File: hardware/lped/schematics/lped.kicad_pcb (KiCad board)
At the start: 4 copper layers, 14 x 14 mm, 30 parts, among them J1 3V3, J10 SWDIO, J2 DOCK_BUTTON, J3 DOCK_CONN, J4 DOCK_LED, J5 GND, J6 ~{RESET}, J9 SWDCLK, U1 nRF52810-QCxx, U2 FXLS8974CF, Y1 32MHz

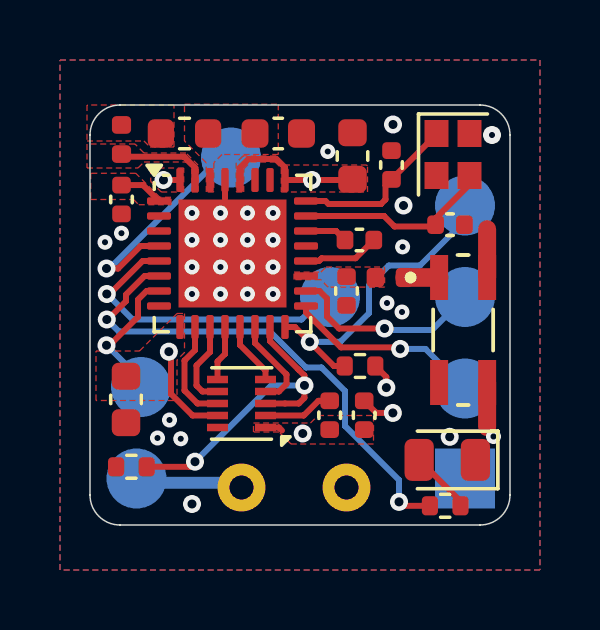
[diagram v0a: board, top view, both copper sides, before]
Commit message: feat(hardware)!: v2 of LPED PCB
* Changed MCU to nRF52833 (from nRF52810)
* Added second LED
* Used specialized filter instead of discrete components for ANT
* Removed unnecessary pull-down resistor from miso
* Removed DOCK_BTN
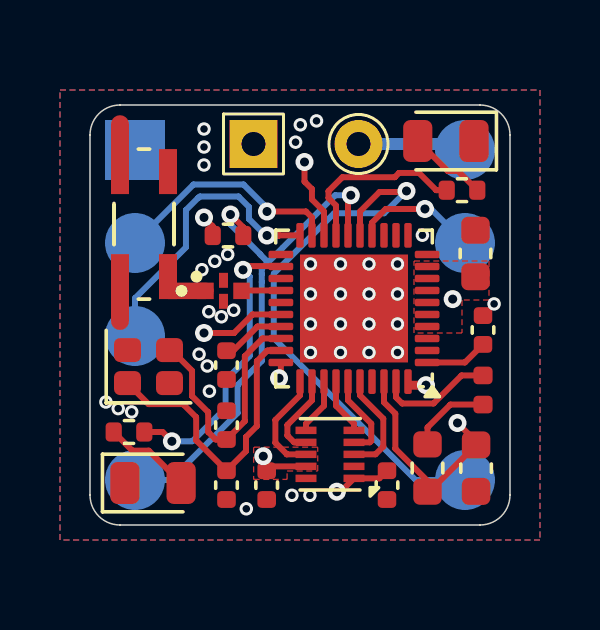
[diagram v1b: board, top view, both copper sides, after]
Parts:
- removed C10: 0u1, Capacitor_SMD:C_0402_1005Metric
- removed C11: 1u, Capacitor_SMD:C_0402_1005Metric
- removed the C3 at (166.1, 72.5)
- removed the J2 at (157.7, 79.9)
- removed L1: 3n9, Inductor_SMD:L_0402_1005Metric
- removed L2: 10u, Inductor_SMD:L_0603_1608Metric
- removed R5: 10k, Resistor_SMD:R_0402_1005Metric
- added C1: 12pF, Capacitor_SMD:C_0402_1005Metric, F.Cu at (160.6, 81.2)
- added D2: LED, Diode_SMD:D_0805_2012Metric, F.Cu at (167.9, 71.7)
- added F1: 2450FM07B0037, RF_Filter:FIL_2450FM07D0034T, F.Cu at (160.4, 76.7)
- added L4: 15n, Inductor_SMD:L_0402_1005Metric, F.Cu at (169.1, 80.0)
- added R3: 2k1, Resistor_SMD:R_0402_1005Metric, F.Cu at (168.4, 73.3)
- C5: value 100p -> 0u1
- C6: value 0p8 -> 100p
- C7: footprint Capacitor_SMD:C_0603_1608Metric -> Capacitor_SMD:C_0402_1005Metric
- C8: value 4u7 -> 1u
- C9: value 1u -> 4u7
- L3: value 15n -> 10u; footprint Inductor_SMD:L_0402_1005Metric -> Inductor_SMD:L_0603_1608Metric
- U1: value nRF52810-QCxx -> nRF52833_QDxx; footprint Package_DFN_QFN:QFN-32-1EP_5x5mm_P0.5mm_EP3.6x3.6mm -> Package_DFN_QFN:QFN-40-1EP_5x5mm_P0.4mm_EP3.6x3.6mm
- moved J7 15.5 mm to (157.5, 72.0)
- moved J4 15.5 mm to (168.5, 72.0)
- moved L3 15.0 mm to (167.2, 82.6), turned to 90 degrees
- moved J1 14.3 mm to (157.5, 83.0)
- moved C4 12.8 mm to (169.1, 78.0), turned to -90 degrees
- moved Y1 12.4 mm to (157.9, 79.2), turned to 0 degrees
- moved C7 12.3 mm to (165.9, 83.2), turned to -90 degrees
- moved C8 11.9 mm to (168.9, 82.6)
- moved C3 11.5 mm to (161.4, 71.8)
- moved C2 11.4 mm to (160.6, 83.2), turned to 90 degrees
- moved AE1 11.2 mm to (157.8, 74.5), turned to -90 degrees
- moved J3 11.1 mm to (157.5, 75.1)
- moved J2 11.1 mm to (157.5, 78.2)
- moved R2 10.8 mm to (157.3, 81.4), turned to 180 degrees
- moved D1 9.84 mm to (158.1, 83.1), turned to 0 degrees
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- renumbered C1 to C3, J6 to J1, J9 to J2, J10 to J3, J1 to J4, J3 to J5, J4 to J6, J5 to J7
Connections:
- C2 pad 2: /XC1 -> /XC2
- C5 pad 1: Earth -> +3V3
- C5 pad 2: /DEC3 -> Earth
- C6 pad 1: /ANT -> Earth
- C6 pad 2: Earth -> /DEC3
- C7 pad 1: Earth -> +3V3
- C7 pad 2: /DEC4 -> Earth
- C8 pad 2: +3V3 -> /DEC4
- C9 pad 1: +3V3 -> Earth
- C9 pad 2: Earth -> +3V3
- L3 pad 1: Net-(L2-Pad2) -> /DEC4
- L3 pad 2: Net-(U1-DCC) -> Net-(L3-Pad2)
- R2 pad 1: /LED -> /LED2
- U1 pad 10: /Accelerometer/INT1 -> Earth
- U1 pad 11: /Accelerometer/CSB -> unconnected-(U1-DECUSB-Pad11)
- U1 pad 12: /Accelerometer/INT2 -> unconnected-(U1-D--Pad12)
- U1 pad 13: /Accelerometer/SCL -> unconnected-(U1-D+-Pad13)
- U1 pad 14: /Accelerometer/MOSI -> /DOCK_CONN
- U1 pad 15: /Accelerometer/MISO -> /DOCK_LED
- U1 pad 17: /SWDCLK -> /LED1
- U1 pad 18: /SWDIO -> +3V3
- U1 pad 19: /ANT -> /SWDIO
- U1 pad 20: Earth -> /SWDCLK
- U1 pad 22: /DEC3 -> /LED2
- U1 pad 23: /XC1 -> unconnected-(U1-NFC2/P0.10-Pad23)
- U1 pad 24: /XC2 -> /ANT
- U1 pad 25: +3V3 -> Earth
- U1 pad 26: unconnected-(U1-P0.25-Pad26) -> /DEC4
- U1 pad 27: unconnected-(U1-P0.28/AIN4-Pad27) -> /DEC3
- U1 pad 28: +3V3 -> /XC1
- U1 pad 29: Earth -> /XC2
- U1 pad 30: /DEC4 -> +3V3
- U1 pad 31: Net-(U1-DCC) -> /Accelerometer/INT1
- U1 pad 32: +3V3 -> /Accelerometer/CSB
- U1 pad 33: Earth -> /Accelerometer/INT2
- U1 pad 4: /DOCK_CONN -> +3V3
- U1 pad 5: /DOCK_LED -> unconnected-(U1-AIN3/P0.05-Pad5)
- U1 pad 6: /LED -> unconnected-(U1-P1.09-Pad6)
- U1 pad 7: /DOCK_BUTTON -> unconnected-(U1-P0.11-Pad7)
- U1 pad 8: /BUZZER -> +3V3
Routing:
- net /DEC4: track 0.00 -> 26.1 mm, vias 0 -> 2
- net /LED: track 16.9 -> 0.00 mm, vias 2 -> 0
- net /LED2: track 0.00 -> 9.65 mm, vias 0 -> 2
- net /DOCK_LED: track 10.5 -> 18.7 mm
- net /~{RESET}: track 10.4 -> 18.0 mm, vias 1 -> 2
- net /Accelerometer/MISO: track 10.6 -> 3.57 mm, vias 2 -> 0
- net Earth: track 9.74 -> 3.06 mm, vias 32 -> 39
- net /LED1: track 0.00 -> 6.01 mm
- net +3V3: track 35.6 -> 41.5 mm, vias 5 -> 7
- net /DOCK_BUTTON: track 4.71 -> 0.00 mm, vias 1 -> 0
- net /XC2: track 5.66 -> 9.81 mm
- net /DOCK_CONN: track 7.74 -> 4.18 mm
- net /SWDCLK: track 6.57 -> 9.66 mm
- net Net-(L3-Pad2): track 0.00 -> 2.73 mm
- net Net-(D2-A): track 0.00 -> 2.66 mm
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- removed copper zone on F.Cu, net /ANT
- removed copper zone on F.Cu, net /DEC1
- removed copper zone on F.Cu, net /DEC4
- removed copper zone on F.Cu, net Net-(L2-Pad2)
- removed copper zone on F.Cu, net Net-(U1-DCC)
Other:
- board text added: "CON"
- board text added: "V2.0"
- board text added: "~{RST}"
- board text removed: "BTN"
- board text removed: "CONN"
- board text removed: "RESET"
- board text removed: "V1.0"

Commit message: feat(hardware): replaced LEDs on dice
* Replaced two red LEDs with single RGB LED (LTRB37G-4R4S)
* Added more ground vias
* Removed DOCK_LED
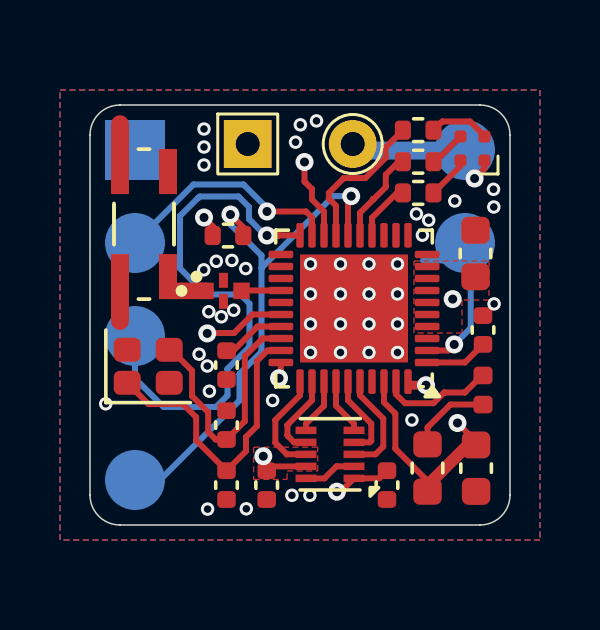
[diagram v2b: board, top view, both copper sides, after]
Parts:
- removed D1, D2: LED, Diode_SMD:D_0805_2012Metric
- removed J6: DOCK_LED, TestPoint:TestPoint_Pad_D2.0mm
- removed R2, R3: 2k1, Resistor_SMD:R_0402_1005Metric
- added D3: LED_RGBA, LED_SMD:LED_Wurth_150044M155260, F.Cu at (168.8, 72.0)
- added R4: 1k, Resistor_SMD:R_0402_1005Metric, F.Cu at (166.9, 73.4)
- added R5: 1k, Resistor_SMD:R_0402_1005Metric, F.Cu at (166.9, 72.4)
- added R6: 1k, Resistor_SMD:R_0402_1005Metric, F.Cu at (166.9, 71.3)
- moved C3 0.19 mm to (161.3, 71.8)
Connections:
- U1 pad 14: /DOCK_CONN -> /LED_R
- U1 pad 15: /DOCK_LED -> /LED_B
- U1 pad 17: /LED1 -> /LED_G
- U1 pad 2: unconnected-(U1-XL1/P0.00-Pad2) -> /DOCK_CONN
- U1 pad 22: /LED2 -> unconnected-(U1-NFC1/P0.09-Pad22)
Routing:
- net /DOCK_LED: track 18.7 -> 0.00 mm, vias 1 -> 0
- net /LED2: track 9.65 -> 0.00 mm, vias 2 -> 0
- net /SWDCLK: track 9.66 -> 18.0 mm
- net /LED1: track 6.01 -> 0.00 mm
- net /LED_G: track 0.00 -> 5.05 mm
- net +3V3: track 41.5 -> 44.6 mm, vias 7 -> 8
- net /LED_B: track 0.00 -> 3.17 mm
- net Net-(D1-A): track 2.95 -> 0.00 mm
- net Net-(D2-A): track 2.66 -> 0.00 mm
- net /DOCK_CONN: track 4.18 -> 6.32 mm
- net Net-(D3-GK): track 0.00 -> 2.04 mm
- net /LED_R: track 0.00 -> 1.96 mm
- net Net-(D3-RK): track 0.00 -> 1.68 mm
- net Earth: track 3.06 -> 4.66 mm, vias 39 -> 46
- net Net-(D3-BK): track 0.00 -> 1.25 mm

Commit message: fix(hardware): LPED PCB clean up
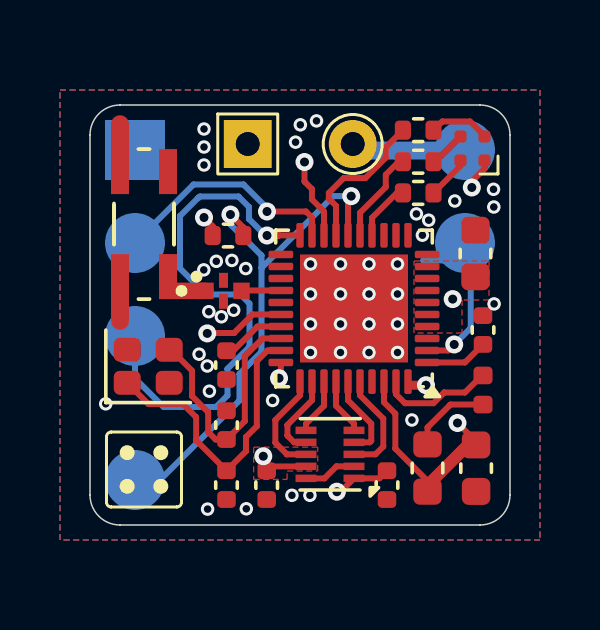
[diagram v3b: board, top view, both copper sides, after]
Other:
- board text removed: "LED"

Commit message: feat(hardware): new 3D models for dice
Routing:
- net /DOCK_CONN: track 6.32 -> 5.50 mm
